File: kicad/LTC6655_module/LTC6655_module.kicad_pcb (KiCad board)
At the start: 2 copper layers, 20.8 x 15.7 mm, 3 parts, among them J1 PINS_1X6, J2 PINS_1X6, M1 LTC6655LS8

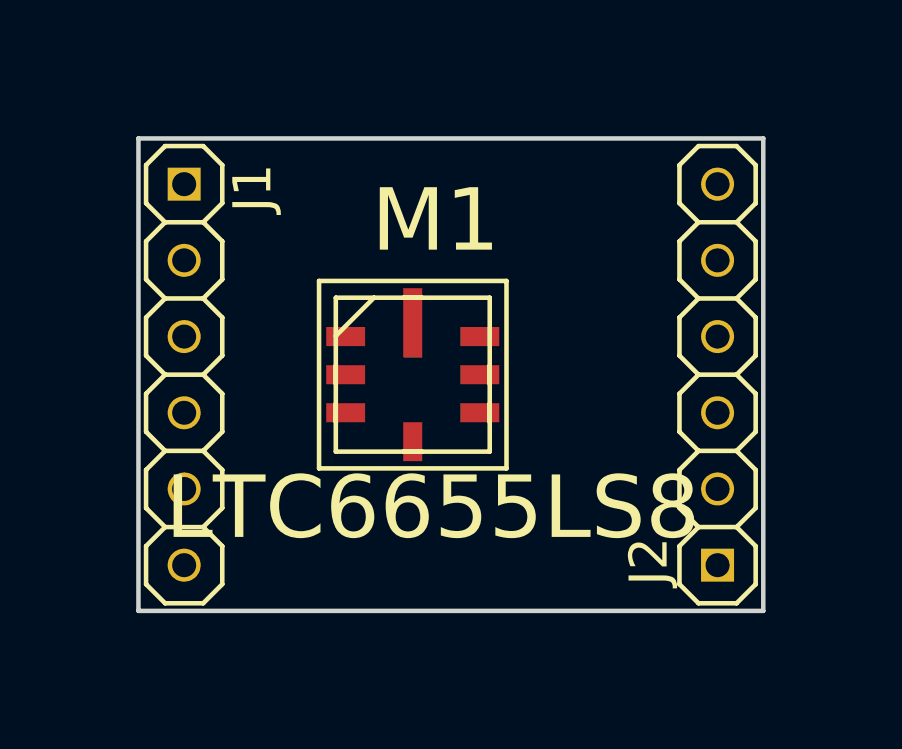
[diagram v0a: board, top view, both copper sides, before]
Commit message: * updated the LTC6655 reference board
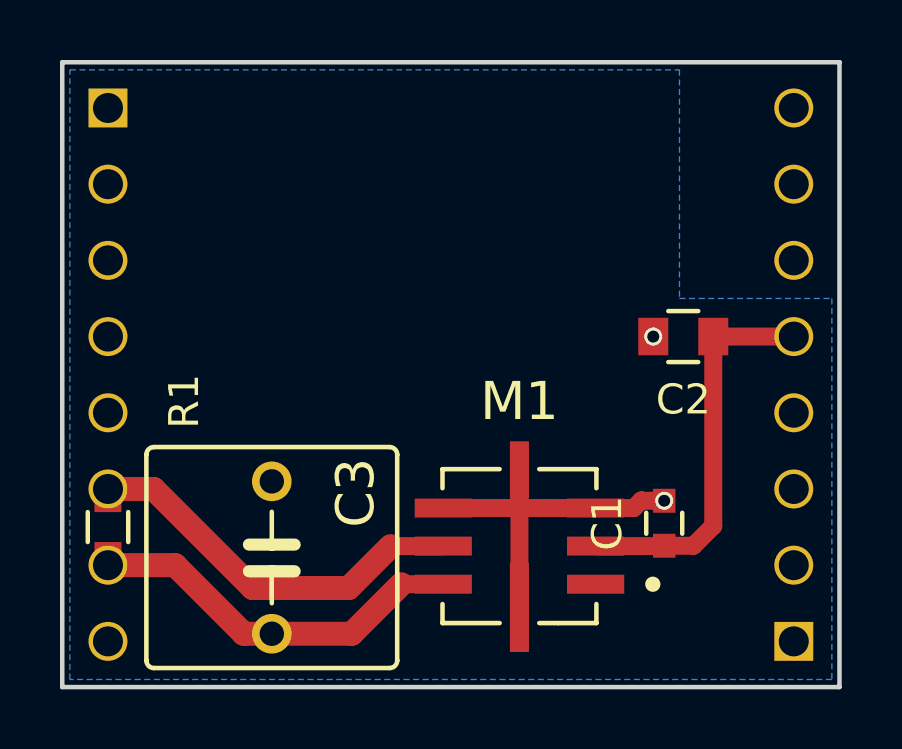
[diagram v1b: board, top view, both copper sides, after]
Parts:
- added C1: 1u, Capacitors_SMD:C_0603, F.Cu at (155.7, 111.6)
- added C2: 10n, Capacitors_SMD:C_0805, F.Cu at (156.3, 105.4)
- added C3: 6.8u, SquantorRcl:C050-085X075, F.Cu at (142.6, 112.8)
- added R1: 0, Resistors_SMD:R_0603, F.Cu at (137.2, 111.8)
- J1, J2: value PINS_1X6 -> PINS_1X8; footprint SquantorConnectors:Header-2.54-1X06-H0.8 -> SquantorConnectors:Header-0254-1X08-H010; moved to B.Cu
- M1: footprint SquantorLinearTechnology:SquantorLinearTechnology-LS8 -> SquantorLinearTechnology:LS8_ELONG
- moved M1 6.73 mm to (150.9, 112.4), turned to 180 degrees
- moved J2 2.54 mm to (160.0, 106.7)
- moved J1 2.54 mm to (137.2, 106.7)
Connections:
- J1 pad 1: Net-(J1-Pad1) -> GND
- J1 pad 2: Net-(J1-Pad2) -> GND
- J1 pad 3: Net-(J1-Pad3) -> GND
- J1 pad 4: Net-(J1-Pad4) -> GND
- J1 pad 5: Net-(J1-Pad5) -> GND
- J1 pad 6: GND -> Sense
- J2 pad 1: Net-(J2-Pad1) -> GND
- J2 pad 2: Net-(J2-Pad2) -> GND
- J2 pad 3: Net-(J2-Pad3) -> GND
- J2 pad 4: Net-(J2-Pad4) -> (no net)
- J2 pad 5: Net-(J2-Pad5) -> Vin
- J2 pad 6: Net-(J2-Pad6) -> HeaterGround
- M1 pad 1: Net-(M1-Pad1) -> (no net)
- M1 pad 2: Net-(M1-Pad2) -> Vin
- M1 pad 6: Net-(M1-Pad6) -> Sense
- M1 pad 7: Net-(M1-Pad7) -> Vref
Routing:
- net Sense: track 0.00 -> 13.6 mm
- net Vref: track 0.00 -> 13.3 mm
- net Vin: track 0.00 -> 13.2 mm
- net GND: track 0.00 -> 12.1 mm, vias 0 -> 2
- added copper zone on B.Cu, net GND
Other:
- board size 20.8 x 15.7 mm -> 25.9 x 20.8 mm
- rule pad_to_mask_clearance: 0.2 -> 0.1

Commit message: * some small modifications
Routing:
- added copper zone on B.Cu, net HeaterGround
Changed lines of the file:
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@@
   (general
     (links 24)
-    (no_connects 13)
+    (no_connects 1)
     (area 135.560999 96.190999 161.619001 117.169001)
     (thickness 1.6)
@@
   )
   (setup
-    (last_trace_width 0.6)
+    (last_trace_width 0.25)
     (user_trace_width 0.2)
     (user_trace_width 0.4)
@@
   (segment (start 153.416 111.125) (end 151.8635 111.125) (width 0.6) (layer F.Cu) (net 1))
   (segment (start 151.8635 111.125) (end 150.876 111.125) (width 0.6) (layer F.Cu) (net 1))
+  (segment (start 137.16 113.03) (end 137.16 112.51) (width 0.25) (layer F.Cu) (net 2))
   (segment (start 146.939 113.665) (end 148.336 113.665) (width 0.6) (layer F.Cu) (net 2))
-  (segment (start 137.16 113.03) (end 137.16 112.51) (width 0.4) (layer F.Cu) (net 2))
   (segment (start 142.621 115.316) (end 141.687054 115.316) (width 0.8) (layer F.Cu) (net 2))
   (segment (start 141.687054 115.316) (end 139.401054 113.03) (width 0.8) (layer F.Cu) (net 2))
@@
       )
     )
+  )
+  (zone (net 5) (net_name HeaterGround) (layer B.Cu) (hatch edge 0.508)
+    (connect_pads (clearance 0.508))
+    (min_thickness 0.254)
+    (fill yes (arc_segments 16) (thermal_gap 0.508) (thermal_bridge_width 0.508))
+    (polygon
+      (pts
+        (xy 161.29 103.505) (xy 156.845 103.505) (xy 156.845 99.06) (xy 161.29 99.06)
+      )
+    )
